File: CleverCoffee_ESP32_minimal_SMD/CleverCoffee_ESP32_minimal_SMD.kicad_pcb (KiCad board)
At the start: 2 copper layers, 78.2 x 57.5 mm, 31 parts

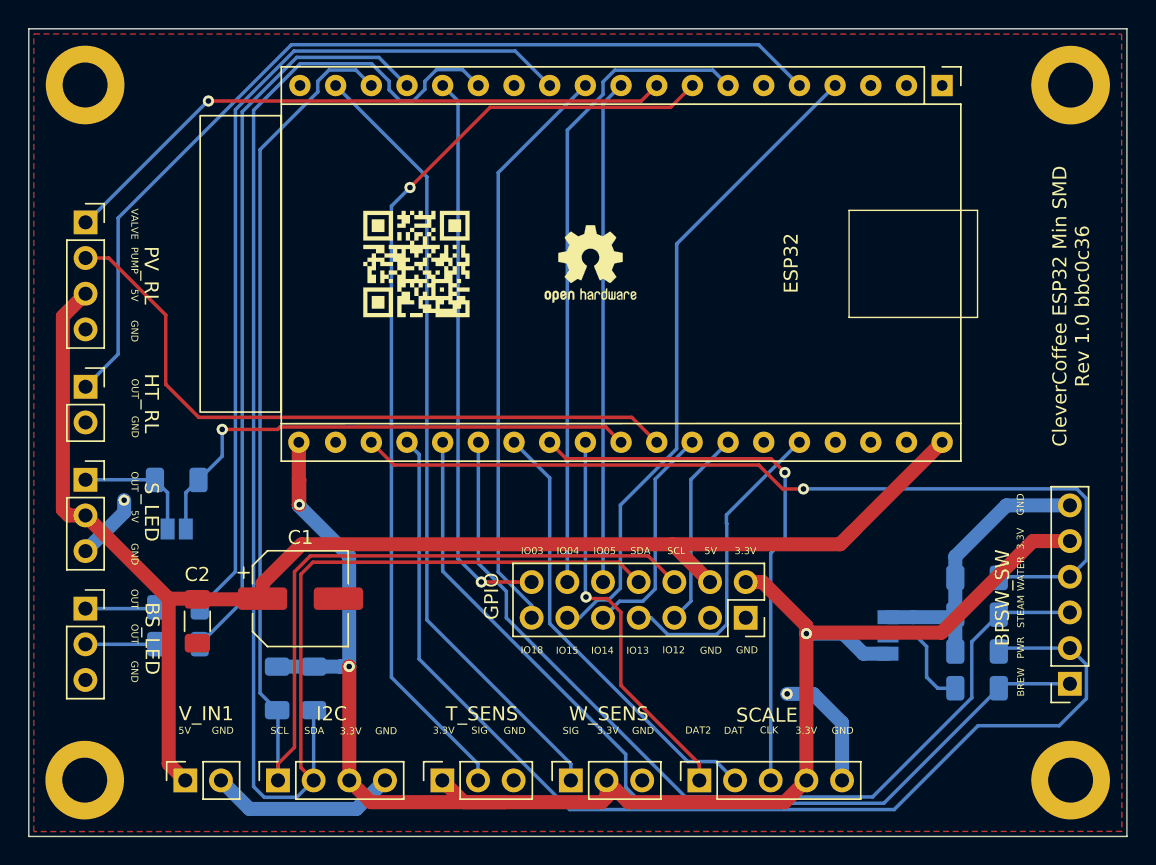
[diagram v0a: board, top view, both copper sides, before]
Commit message: mirrored pin headers to correct GND pad, changed SMD footprints to 0805 and rearranged SMD parts
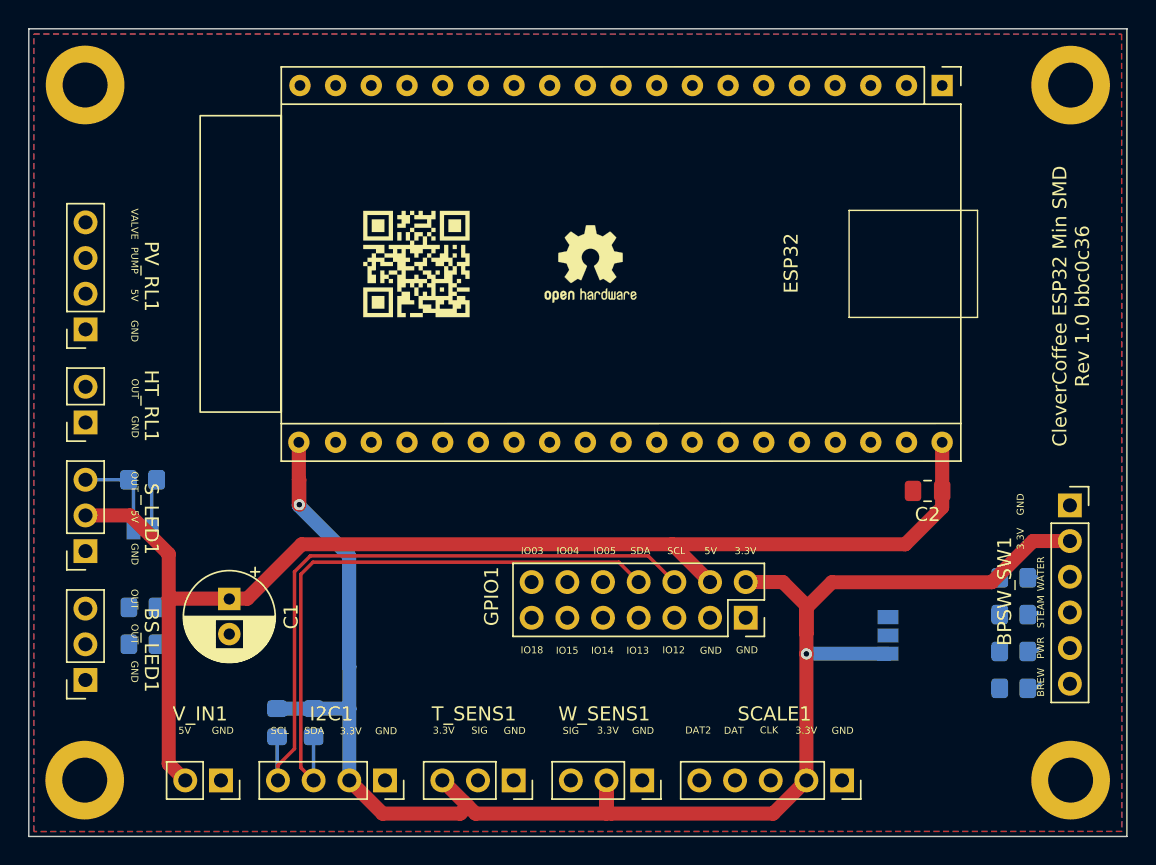
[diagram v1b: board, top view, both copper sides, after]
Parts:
- C1: footprint Capacitor_SMD:CP_Elec_6.3x7.7 -> Capacitor_THT:CP_Radial_D6.3mm_P2.50mm
- C2: footprint Capacitor_SMD:C_1206_3216Metric_Pad1.33x1.80mm_HandSolder -> Capacitor_SMD:C_0805_2012Metric_Pad1.18x1.45mm_HandSolder
- R1, R2, R3, R4, R5, R6, R7, R8, R9: footprint Resistor_SMD:R_1206_3216Metric_Pad1.30x1.75mm_HandSolder -> Resistor_SMD:R_0805_2012Metric_Pad1.20x1.40mm_HandSolder
- moved C2 52.8 mm to (163.8, 107.9), turned to 180 degrees
- moved BPSW_SW1 12.7 mm to (173.9, 108.9), turned to 0 degrees
- moved SCALE1 10.2 mm to (157.7, 128.5), turned to -90 degrees
- moved PV_RL1 7.62 mm to (103.8, 96.4), turned to 180 degrees
- moved I2C1 7.62 mm to (125.2, 128.5), turned to -90 degrees
- moved W_SENS1 5.08 mm to (143.5, 128.5), turned to -90 degrees
- moved BS_LED1 5.08 mm to (103.8, 121.3), turned to 180 degrees
- moved S_LED1 5.08 mm to (103.8, 112.2), turned to 180 degrees
- moved T_SENS1 5.08 mm to (134.3, 128.5), turned to -90 degrees
- moved C1 5.07 mm to (114.1, 115.6), turned to -90 degrees
- moved R3 2.61 mm to (169.9, 121.9)
- moved R4 2.61 mm to (169.9, 114.1)
- moved R5 2.61 mm to (169.9, 119.3)
- moved R9 2.61 mm to (169.9, 116.7)
- moved HT_RL1 2.54 mm to (103.8, 103.0), turned to 180 degrees
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- renumbered BPSW_SW to BPSW_SW1, BS_LED to BS_LED1, GPIO to GPIO1, HT_RL to HT_RL1, I2C to I2C1, PV_RL to PV_RL1, SCALE to SCALE1, S_LED to S_LED1, T_SENS to T_SENS1, W_SENS to W_SENS1
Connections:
- BPSW_SW1 pad 1: IO34 -> GND
- BPSW_SW1 pad 2: IO39 -> +3V3
- BPSW_SW1 pad 3: IO35 -> IO36
- BPSW_SW1 pad 4: IO36 -> IO35
- BPSW_SW1 pad 5: +3V3 -> IO39
- BPSW_SW1 pad 6: GND -> IO34
- BS_LED1 pad 1: Net-(BS_LED1-Pin_1) -> GND
- BS_LED1 pad 3: GND -> Net-(BS_LED1-Pin_3)
- HT_RL1 pad 1: IO2 -> GND
- HT_RL1 pad 2: GND -> IO2
- I2C1 pad 1: SCL -> GND
- I2C1 pad 2: SDA -> +3V3
- I2C1 pad 3: +3V3 -> SDA
- I2C1 pad 4: GND -> SCL
- PV_RL1 pad 1: VALVE -> GND
- PV_RL1 pad 2: PUMP -> +5V
- PV_RL1 pad 3: +5V -> PUMP
- PV_RL1 pad 4: GND -> VALVE
- R6 pad 1: Net-(BS_LED1-Pin_1) -> Net-(BS_LED1-Pin_3)
- SCALE1 pad 1: DAT2 -> GND
- SCALE1 pad 2: DAT -> +3V3
- SCALE1 pad 4: +3V3 -> DAT
- SCALE1 pad 5: GND -> DAT2
- S_LED1 pad 1: Net-(JP1-A) -> GND
- S_LED1 pad 3: GND -> Net-(JP1-A)
- T_SENS1 pad 1: +3V3 -> GND
- T_SENS1 pad 3: GND -> +3V3
- V_IN1 pad 1: +5V -> GND
- V_IN1 pad 2: GND -> +5V
- W_SENS1 pad 1: IO23 -> GND
- W_SENS1 pad 3: GND -> IO23
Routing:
- net IO39: track 80.2 -> 0.34 mm
- net SDA: track 118.8 -> 43.2 mm
- net IO16: track 68.4 -> 0.00 mm, vias 1 -> 0
- net IO2: track 67.8 -> 0.00 mm
- net IO35: track 66.5 -> 0.23 mm
- net IO34: track 65.6 -> 0.45 mm
- net IO36: track 63.7 -> 0.11 mm, vias 1 -> 0
- net IO19: track 61.6 -> 0.13 mm
- net IO23: track 56.4 -> 0.00 mm
- net SCL: track 100.2 -> 46.8 mm
- net IO1: track 53.3 -> 0.01 mm
- net PUMP: track 49.0 -> 0.00 mm
- net GND: track 48.3 -> 0.00 mm, vias 2 -> 0
- net IO15: track 46.8 -> 0.00 mm
- net IO4: track 46.4 -> 0.00 mm
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- added copper zone on B.Cu, net GND

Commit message: first routing draft
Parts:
- ESP32: footprint Module:NodeMCU DevKitC v4 -> symbols:NodeMCU DevKitC v4
- moved JP1 6.20 mm to (107.9, 104.4)
- moved JP2 5.31 mm to (165.0, 121.6)
- moved C2 2.06 mm to (165.8, 107.9), turned to 0 degrees
- moved C1 1.67 mm to (113.0, 116.8), turned to 0 degrees
- moved R3 0.33 mm to (169.9, 121.6)
- moved R5 0.25 mm to (169.9, 119.1)
- moved R9 0.17 mm to (169.9, 116.5)
- moved R6 0.08 mm to (107.9, 116.3)
- moved R4 0.06 mm to (169.9, 114.0)
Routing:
- net IO2: track 0.00 -> 73.6 mm, vias 0 -> 2
- net IO16: track 0.00 -> 71.0 mm, vias 0 -> 3
- net IO23: track 0.00 -> 63.5 mm, vias 0 -> 2
- net IO19: track 0.13 -> 63.3 mm, vias 0 -> 2
- net SCL: track 46.8 -> 105.0 mm, vias 0 -> 2
- net IO36: track 0.11 -> 58.2 mm, vias 0 -> 1
- net IO15: track 0.00 -> 57.2 mm, vias 0 -> 1
- net IO34: track 0.45 -> 57.6 mm, vias 0 -> 1
- net IO39: track 0.34 -> 57.4 mm, vias 0 -> 1
- net IO1: track 0.01 -> 55.7 mm, vias 0 -> 2
- net IO35: track 0.23 -> 51.8 mm, vias 0 -> 1
- net PUMP: track 0.00 -> 50.9 mm, vias 0 -> 1
- net VALVE: track 0.07 -> 50.5 mm, vias 0 -> 1
- net IO4: track 0.00 -> 50.1 mm, vias 0 -> 1
- net SDA: track 43.2 -> 90.8 mm, vias 0 -> 2
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
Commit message: improved routing, added gnd plane stitching
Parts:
- moved C1 0.85 mm to (113.0, 117.7)
- moved JP2 0.80 mm to (164.2, 121.6)
- renumbered BPSW_SW1 to BPSW_SW, BS_LED1 to BS_LED, GPIO1 to GPIO, HT_RL1 to HT_RL, I2C1 to I2C, PV_RL1 to PV_RL, SCALE1 to SCALE, S_LED1 to S_LED, T_SENS1 to T_SENS, V_IN1 to V_IN, W_SENS1 to W_SENS
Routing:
- net SDA: track 90.8 -> 87.2 mm, vias 2 -> 3
- net SCL: track 105.0 -> 101.5 mm, vias 2 -> 3
- net IO3: track 38.0 -> 41.0 mm, vias 0 -> 1
- net +3V3: track 126.7 -> 128.5 mm, vias 2 -> 4
- net IO2: track 73.6 -> 72.7 mm
- net IO18: track 44.7 -> 43.8 mm
- net Net-(JP2-C): track 3.91 -> 4.72 mm
- net IO26: track 39.7 -> 40.5 mm
- net VALVE: track 50.5 -> 49.9 mm
- net IO16: track 71.0 -> 71.6 mm
- net +5V: track 112.1 -> 112.6 mm
- net GND: vias 9 -> 79
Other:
- board text added: "CleverCoffee ESP32 Min SMD Modified by sophyx"
- board text removed: "CleverCoffee ESP32 Min SMD Rev 1.0 bbc0c36"
